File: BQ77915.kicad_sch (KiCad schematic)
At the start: 24 parts, among them U1 BQ7791500PWR, U3 MCP6001-OT, U4 INA181A1

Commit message: fix silkscreen issues and start implementing small layout improvements, cleanup repo
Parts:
- renumbered BT2 to BT1, BT1 to BT2

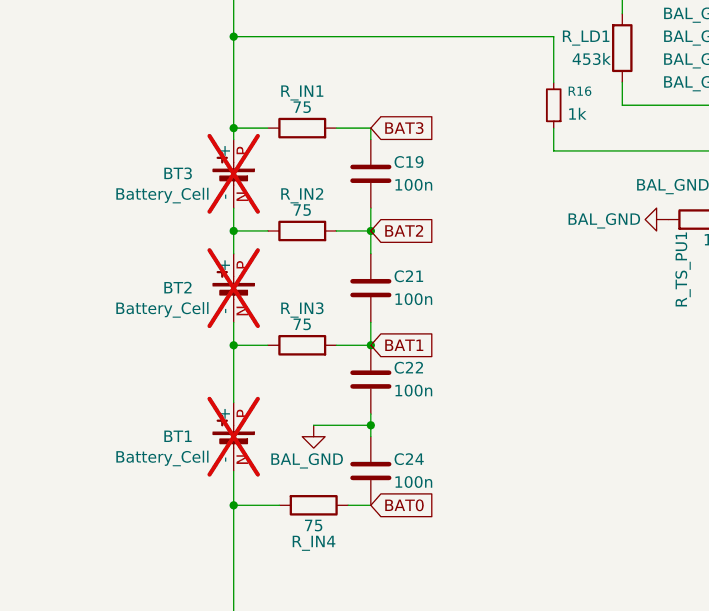
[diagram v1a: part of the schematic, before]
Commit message: current state, shrinked board, some adaptions still neccesarry
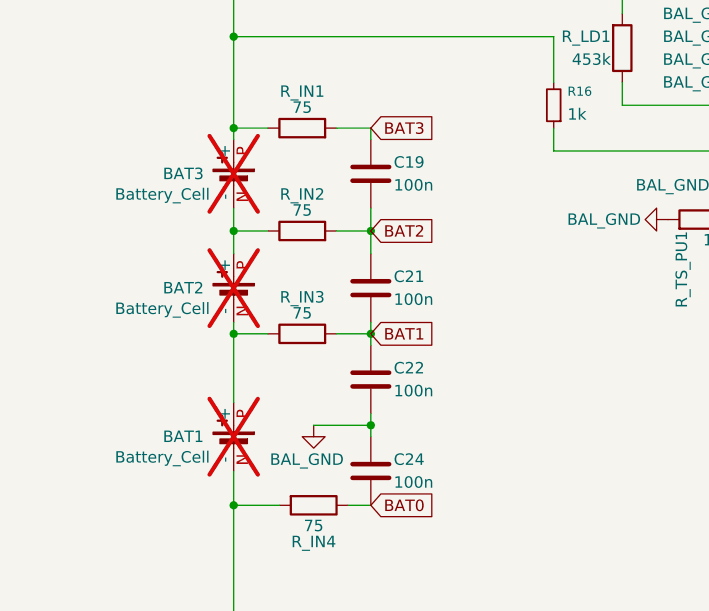
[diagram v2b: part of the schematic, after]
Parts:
- renumbered BT1 to BAT1, BT2 to BAT2, BT3 to BAT3
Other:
- moved on the sheet: R_IN3
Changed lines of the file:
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@@
 	)
 	(junction
-		(at 77.47 132.08)
-		(diameter 0)
-		(color 0 0 0 0)
-	)
-	(junction
 		(at 62.23 149.86)
 		(diameter 0)
@@
 	)
 	(junction
+		(at 62.23 130.81)
+		(diameter 0)
+		(color 0 0 0 0)
+	)
+	(junction
 		(at 198.12 25.4)
 		(diameter 0)
@@
 	)
 	(junction
-		(at 62.23 132.08)
-		(diameter 0)
-		(color 0 0 0 0)
-	)
-	(junction
 		(at 121.92 114.3)
 		(diameter 0)
@@
 	)
 	(junction
+		(at 77.47 130.81)
+		(diameter 0)
+		(color 0 0 0 0)
+	)
+	(junction
 		(at 59.69 67.31)
 		(diameter 0)
@@
 	(wire
 		(pts
-			(xy 62.23 132.08) (xy 62.23 138.43)
+			(xy 62.23 130.81) (xy 62.23 138.43)
 		)
 		(stroke
@@
 	(wire
 		(pts
-			(xy 62.23 132.08) (xy 66.04 132.08)
+			(xy 62.23 130.81) (xy 66.04 130.81)
 		)
 		(stroke
@@
 	(wire
 		(pts
+			(xy 77.47 130.81) (xy 77.47 132.08)
+		)
+		(stroke
+			(width 0)
+			(type default)
+		)
+	)
+	(wire
+		(pts
 			(xy 105.41 102.87) (xy 105.41 105.41)
 		)
@@
 	(wire
 		(pts
-			(xy 62.23 129.54) (xy 62.23 132.08)
+			(xy 62.23 129.54) (xy 62.23 130.81)
 		)
 		(stroke
@@
 	(wire
 		(pts
-			(xy 73.66 132.08) (xy 77.47 132.08)
+			(xy 73.66 130.81) (xy 77.47 130.81)
 		)
 		(stroke
@@
 	(wire
 		(pts
-			(xy 77.47 129.54) (xy 77.47 132.08)
+			(xy 77.47 129.54) (xy 77.47 130.81)
 		)
 		(stroke
@@
 	(global_label "BAT1"
 		(shape input)
-		(at 77.47 132.08 0)
+		(at 77.47 130.81 0)
 		(fields_autoplaced yes)
 		(effects
@@
 		)
 		(property "Intersheetrefs" "${INTERSHEET_REFS}"
-			(at 84.9909 132.08 0)
+			(at 84.9909 130.81 0)
 			(hide yes)
 			(show_name no)
@@
 		(in_pos_files yes)
 		(dnp yes)
-		(property "Reference" "BT1"
+		(property "Reference" "BAT1"
 			(at 54.356 142.24 0)
 			(show_name no)
@@
 			(project "rapid_power_module"
 				(path "/afc8cbd3-9ea8-40a2-afae-ed6bd0fe7e6e/f9ba2c7f-e63c-4860-86c8-ae922535c6b3"
-					(reference "BT1")
+					(reference "BAT1")
 					(unit 1)
 				)
@@
 	(symbol
 		(lib_id "Device:R")
-		(at 69.85 132.08 90)
+		(at 69.85 130.81 90)
 		(unit 1)
 		(body_style 1)
@@
 		(dnp no)
 		(property "Reference" "R_IN3"
-			(at 69.85 128.016 90)
+			(at 69.85 126.746 90)
 			(show_name no)
 			(do_not_autoplace no)
@@
 		)
 		(property "Value" "75"
-			(at 69.85 129.794 90)
+			(at 69.85 128.524 90)
 			(show_name no)
 			(do_not_autoplace no)
@@
 		)
 		(property "Footprint" "Resistor_SMD:R_0603_1608Metric"
-			(at 69.85 133.858 90)
+			(at 69.85 132.588 90)
 			(hide yes)
 			(show_name no)
@@
 		)
 		(property "Datasheet" ""
-			(at 69.85 132.08 0)
+			(at 69.85 130.81 0)
 			(hide yes)
 			(show_name no)
@@
 		)
 		(property "Description" "Resistor"
-			(at 69.85 132.08 0)
+			(at 69.85 130.81 0)
 			(hide yes)
 			(show_name no)
@@
 		)
 		(property "LCSC" "C4275"
-			(at 69.85 132.08 90)
+			(at 69.85 130.81 90)
 			(hide yes)
 			(show_name no)
@@
 		(in_pos_files yes)
 		(dnp yes)
-		(property "Reference" "BT3"
+		(property "Reference" "BAT3"
 			(at 54.356 113.03 0)
 			(show_name no)
@@
 			(project "rapid_power_module"
 				(path "/afc8cbd3-9ea8-40a2-afae-ed6bd0fe7e6e/f9ba2c7f-e63c-4860-86c8-ae922535c6b3"
-					(reference "BT3")
+					(reference "BAT3")
 					(unit 1)
 				)
@@
 		(in_pos_files yes)
 		(dnp yes)
-		(property "Reference" "BT2"
+		(property "Reference" "BAT2"
 			(at 54.356 125.73 0)
 			(show_name no)
@@
 			(project "rapid_power_module"
 				(path "/afc8cbd3-9ea8-40a2-afae-ed6bd0fe7e6e/f9ba2c7f-e63c-4860-86c8-ae922535c6b3"
-					(reference "BT2")
+					(reference "BAT2")
 					(unit 1)
 				)

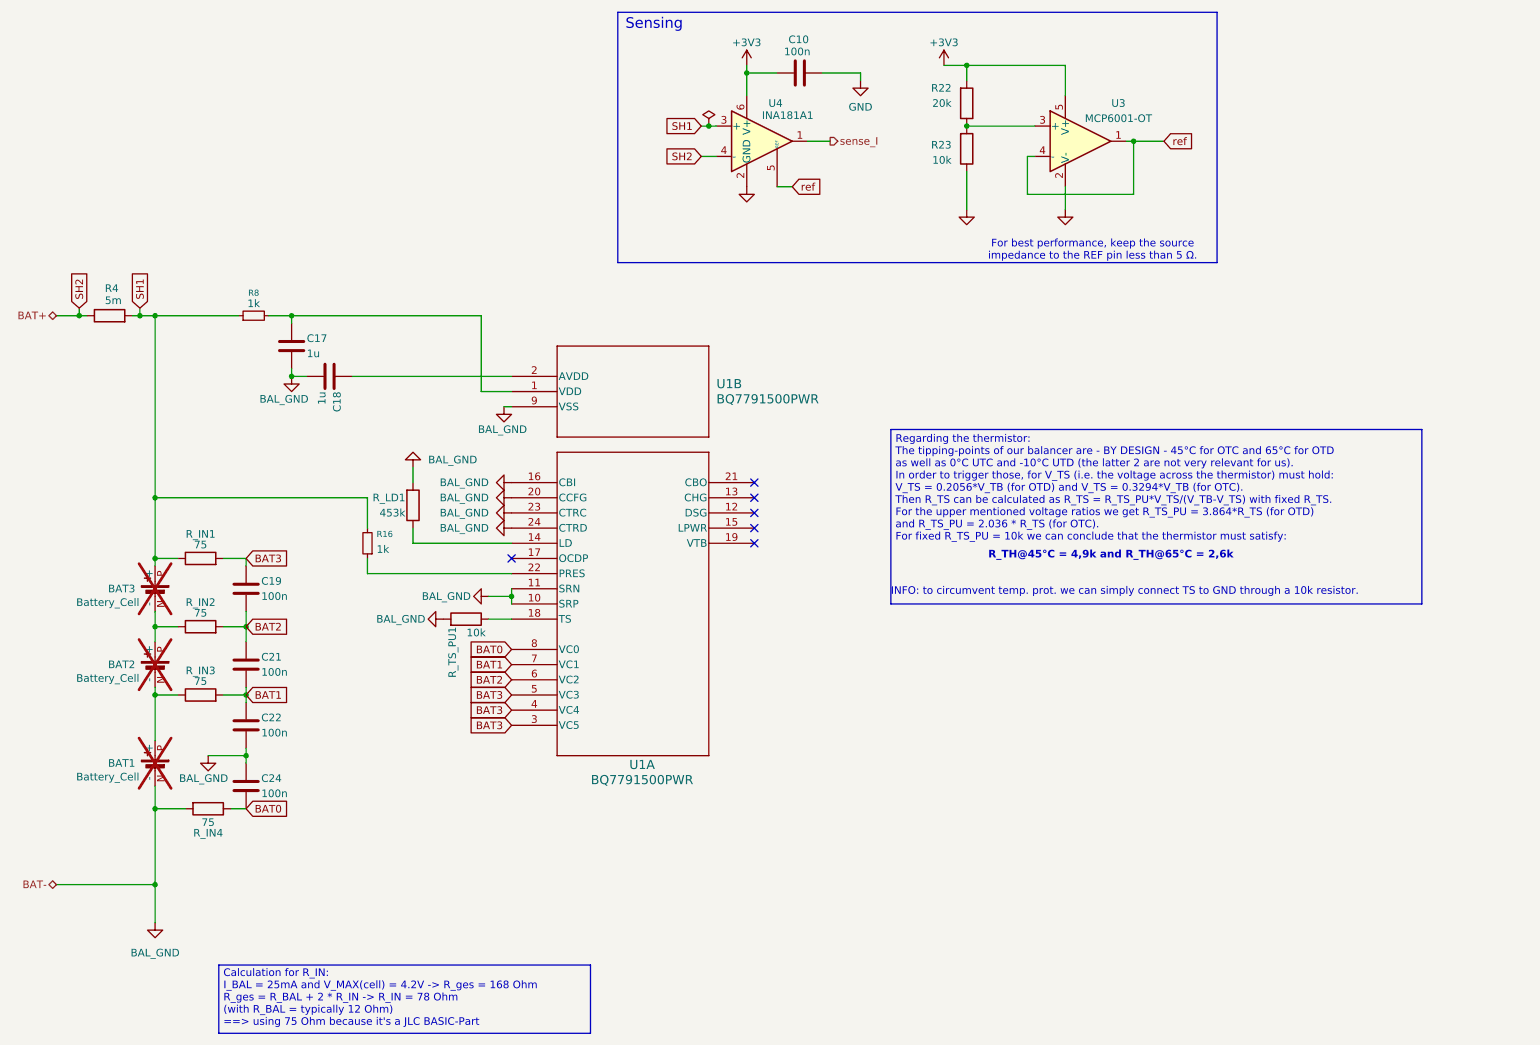
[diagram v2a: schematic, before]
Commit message: finished routing adaptions
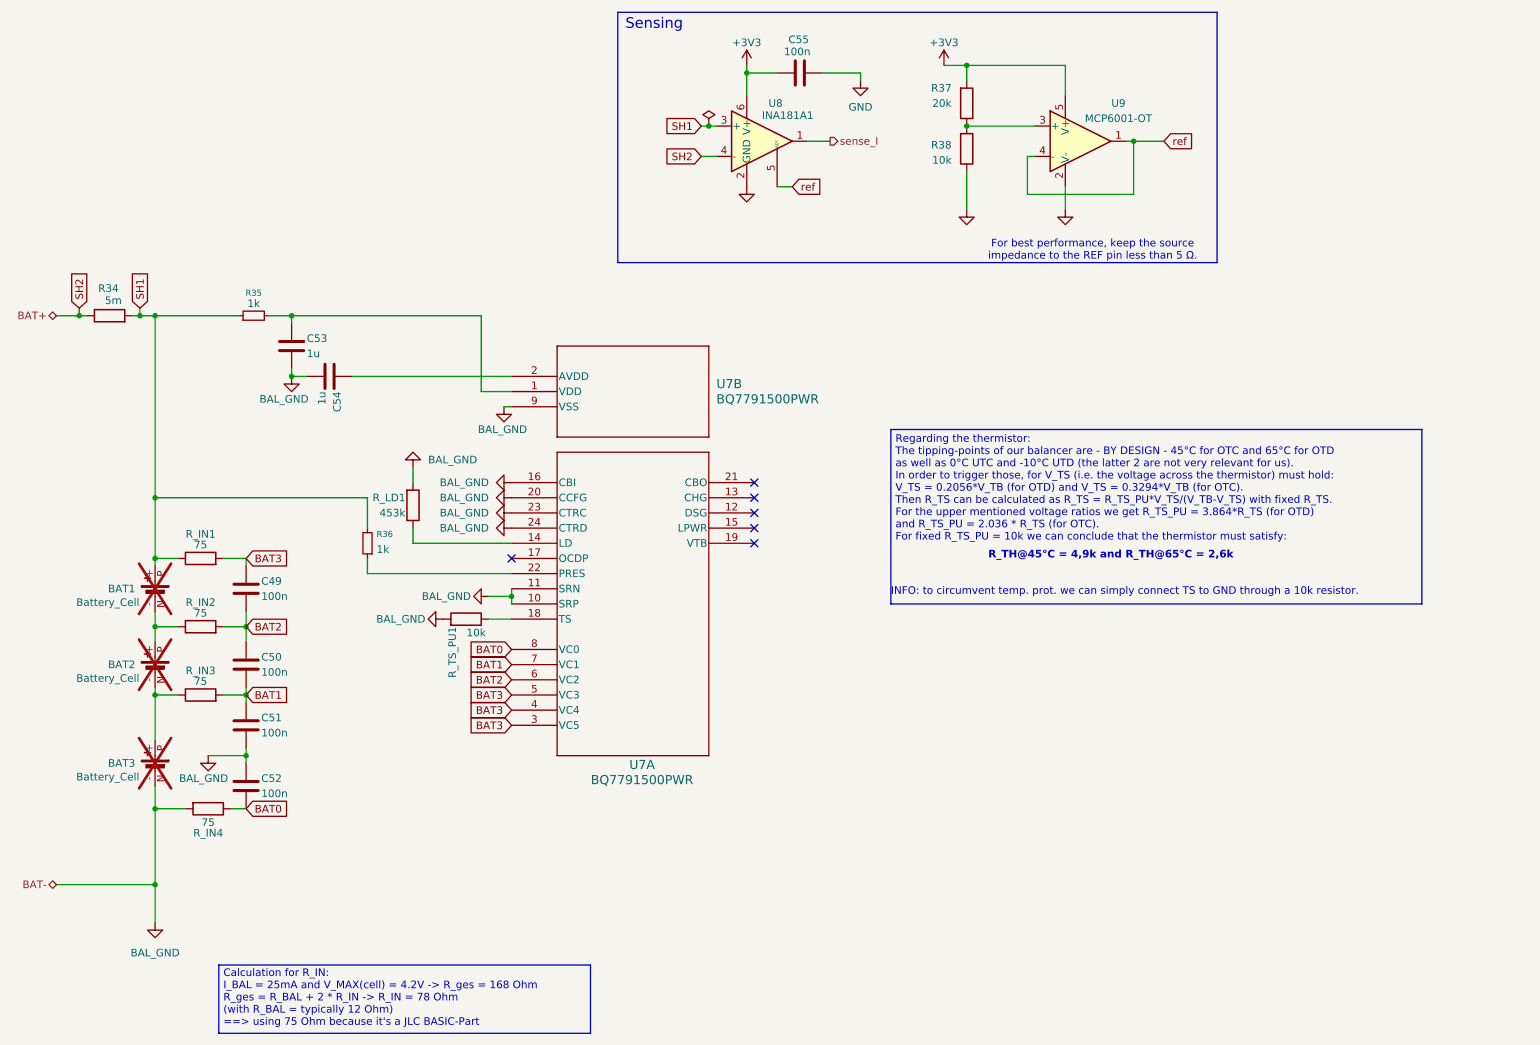
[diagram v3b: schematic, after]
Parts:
- renumbered BAT3 to BAT1, BAT1 to BAT3, C19 to C49, C21 to C50, C22 to C51, C24 to C52, C17 to C53, C18 to C54, C10 to C55, R4 to R34, R8 to R35, R16 to R36, R22 to R37, R23 to R38, U1 to U7, U4 to U8, U3 to U9
